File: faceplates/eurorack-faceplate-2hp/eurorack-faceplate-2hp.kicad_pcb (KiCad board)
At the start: 2 copper layers, 9.8 x 133.3 mm, 2 parts

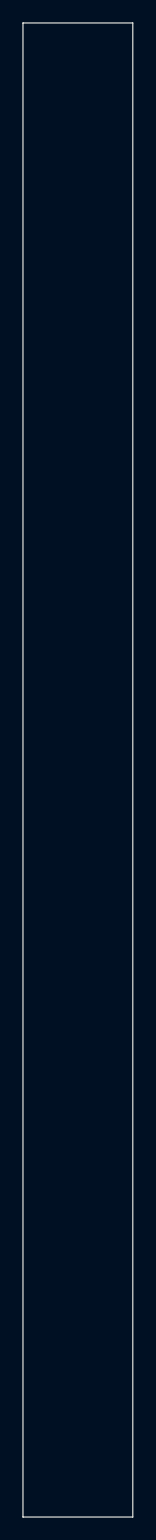
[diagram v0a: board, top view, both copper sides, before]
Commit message: Correcting panel height
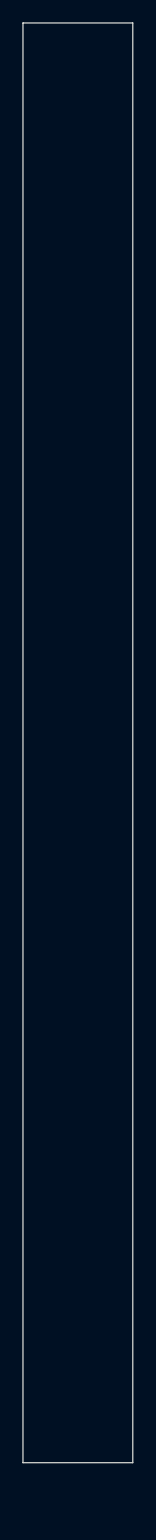
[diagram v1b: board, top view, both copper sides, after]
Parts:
- moved REF** 4.85 mm to (6.15, 125.5)
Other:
- board size 9.8 x 133.3 mm -> 9.8 x 128.5 mm
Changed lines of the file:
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@@
   (net 0 "")
   (footprint "MountingHole:MountingHole_3.2mm_M3" (layer "F.Cu")
-    (at 6.15 130.35)
+    (at 6.15 125.5)
     (descr "Mounting Hole 3.2mm, no annular, M3")
     (tags "mounting hole 3.2mm no annular m3")
@@
     (pad "" np_thru_hole oval locked (at 0 0) (size 6 3.2) (drill oval 6 3.2) (layers F&B.Cu *.Mask))
   )
-  (gr_line (start 9.8 0) (end 9.8 133.35) (layer "Edge.Cuts") (width 0.1))
-  (gr_line (start 0 133.35) (end 0 0) (layer "Edge.Cuts") (width 0.1))
+  (gr_line (start 9.8 0) (end 9.8 128.5) (layer "Edge.Cuts") (width 0.1))
+  (gr_line (start 0 128.5) (end 0 0) (layer "Edge.Cuts") (width 0.1))
   (gr_line (start 0 0) (end 9.8 0) (layer "Edge.Cuts") (width 0.1))
-  (gr_line (start 9.8 133.35) (end 0 133.35) (layer "Edge.Cuts") (width 0.1))
+  (gr_line (start 9.8 128.5) (end 0 128.5) (layer "Edge.Cuts") (width 0.1))
   (dimension (type aligned) (layer "User.1")
     (pts (xy 0 3) (xy 7.5 3))
